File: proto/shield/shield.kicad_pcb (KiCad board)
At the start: 2 copper layers, 68.6 x 124.5 mm, 104 parts, among them J1 ESC_XY, J10 gpio_d, J11 gpio_d, J12 gpio_d, J13 gpio_d, J14 gpio_a, J15 gpio_a, J16 gpio_a, J17 gpio_a, J18 gpio_a, J19 gpio_a, J2 ESC_4Z, J20 gpio_a, J21 gpio_a, J22 5V_IN_A, J23 5V_IN_D, J3 PWM1, J4 PWM2, J5 PWM3, J6 gpio_d, J7 gpio_d, J8 gpio_d, J9 gpio_d, U1 NUCLEO144-F746ZG, U10 LTV-817S, U11 LTV-817S, U12 LTV-817S, U13 LTV-817S, U14 LTV-817S, U15 LTV-817S, U16 LTV-817S, U17 LTV-817S, U2 6N137, U3 6N137, U4 6N137, U5 6N137, U6 6N137, U7 6N137, U8 6N137, U9 6N137

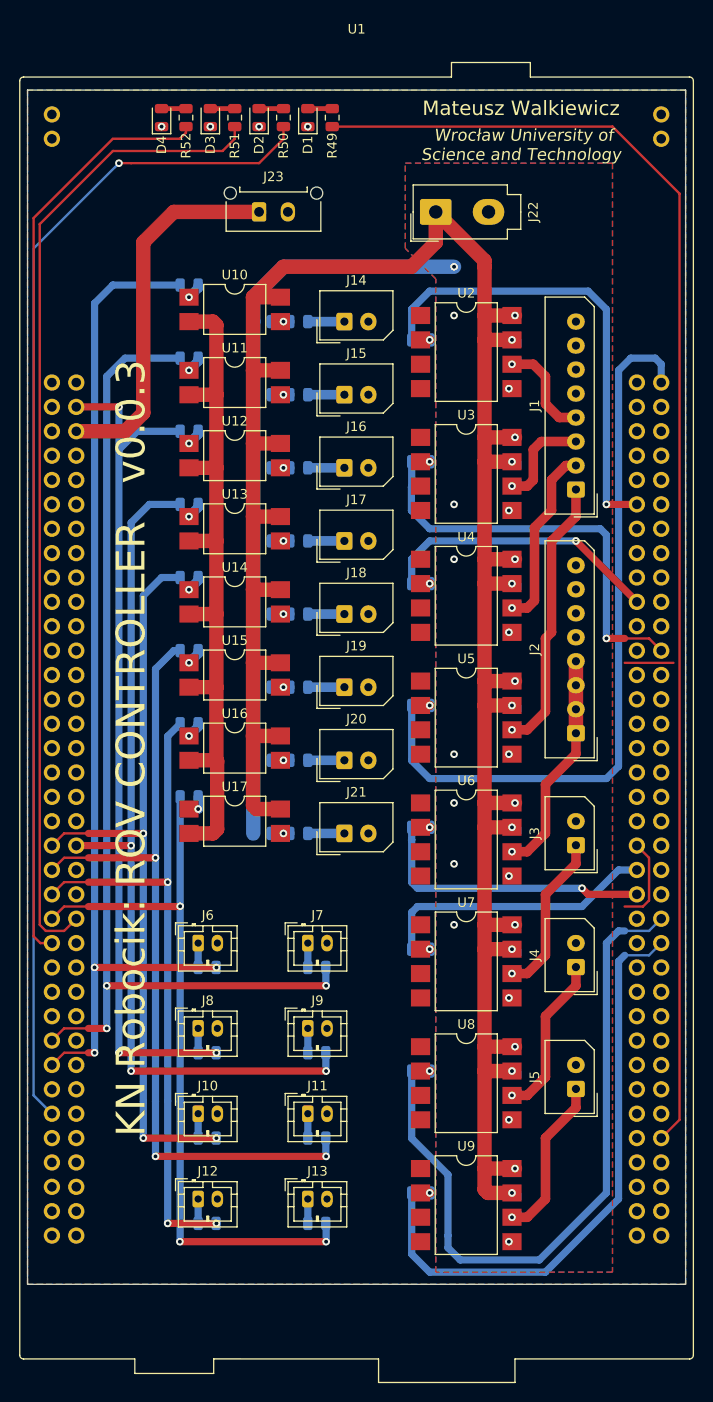
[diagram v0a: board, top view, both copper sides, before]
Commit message: pcb + can + rs232
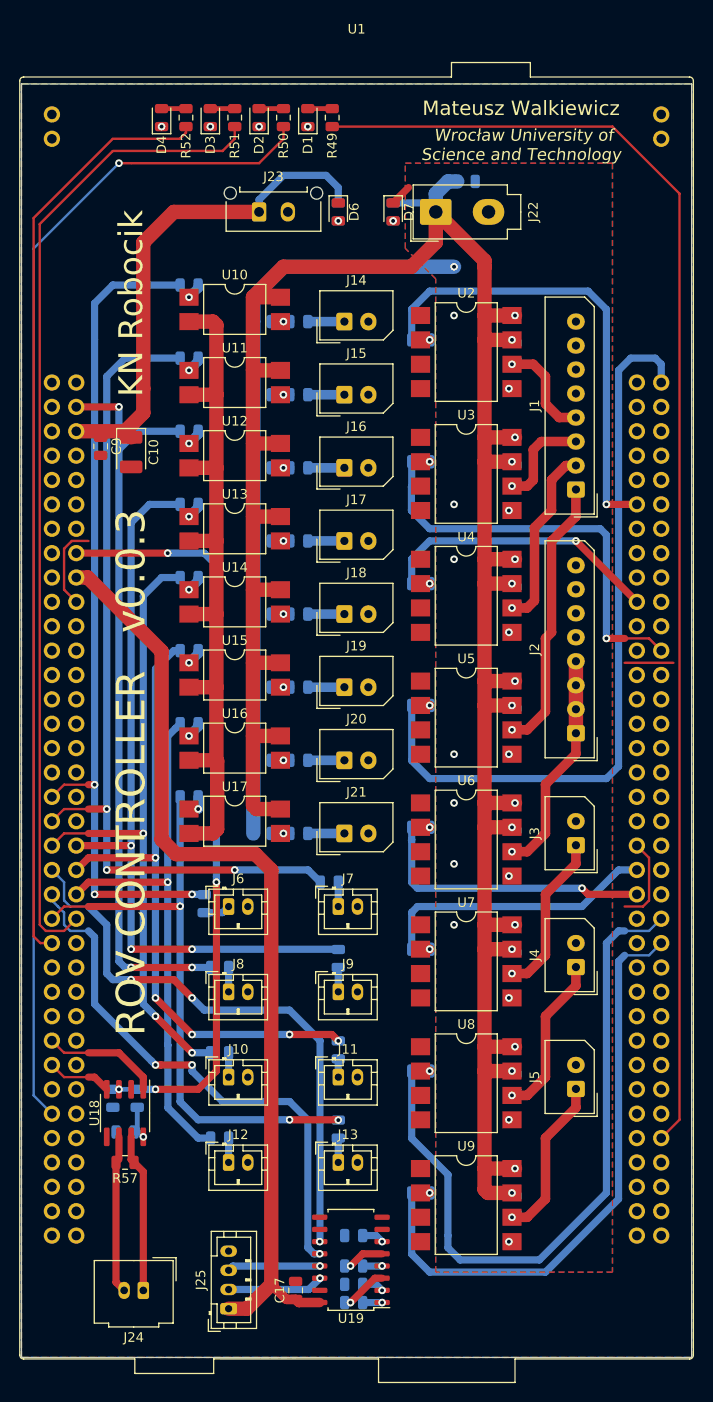
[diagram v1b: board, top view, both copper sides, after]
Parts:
- added C10: 33u, Capacitor_Tantalum_SMD:CP_EIA-3528-21_Kemet-B, F.Cu at (51.4, 78.4)
- added C11: 10u, Capacitor_SMD:C_0805_2012Metric, B.Cu at (86.4, 50.2)
- added C12: 10u, Capacitor_SMD:C_0805_2012Metric, B.Cu at (49.5, 145.7)
- added C13: 47n, Capacitor_SMD:C_0805_2012Metric, B.Cu at (74.6, 167.0)
- added C14: 330n, Capacitor_SMD:C_0805_2012Metric, B.Cu at (74.6, 163.2)
- added C15: 330n, Capacitor_SMD:C_0805_2012Metric, B.Cu at (74.6, 165.1)
- added C16: 330n, Capacitor_SMD:C_0805_2012Metric, B.Cu at (74.6, 160.0)
- added C17: 10u, Capacitor_SMD:C_0805_2012Metric, F.Cu at (68.6, 165.7)
- added C9: 10u, Capacitor_SMD:C_0805_2012Metric, F.Cu at (48.3, 77.8)
- added D6: LED_B, LED_SMD:LED_0805_2012Metric, F.Cu at (73.0, 53.3)
- added D7: LED_B, LED_SMD:LED_0805_2012Metric, F.Cu at (78.7, 53.3)
- added J24: CAN_LINK, Connector_Molex:Molex_MicroClasp_55932-0230_1x02_P2.00mm_Vertical, F.Cu at (52.7, 165.7)
- added J25: Conn_01x04, Connector_JST:JST_PH_B4B-PH-K_1x04_P2.00mm_Vertical, F.Cu at (61.6, 167.6)
- added R53: R, Resistor_SMD:R_0805_2012Metric, B.Cu at (73.0, 53.3)
- added R54: R, Resistor_SMD:R_0805_2012Metric, B.Cu at (78.7, 53.3)
- added R55: 2k2, Resistor_SMD:R_0805_2012Metric, B.Cu at (52.1, 145.7)
- added R56: 10k, Resistor_SMD:R_0805_2012Metric, B.Cu at (50.8, 149.2)
- added R57: 120, Resistor_SMD:R_0805_2012Metric, F.Cu at (50.8, 152.4)
- added U18: SN65HVD230, Package_SO:SOIC-8_3.9x4.9mm_P1.27mm, F.Cu at (50.8, 147.3)
- added U19: MAX3232, Package_SO:SOIC-16_4.55x10.3mm_P1.27mm, F.Cu at (74.3, 162.6)
- U1: value NUCLEO144-F746ZG -> NUCLEO144-F767ZI
- moved R36 10.1 mm to (73.0, 131.1), turned to 90 degrees
- moved R40 10.1 mm to (73.0, 148.9), turned to 90 degrees
- moved R38 9.46 mm to (73.0, 140.7), turned to 90 degrees
- moved R34 8.98 mm to (72.1, 123.2), turned to 180 degrees
- moved R37 8.98 mm to (60.7, 141.0), turned to 180 degrees
- moved R35 8.98 mm to (60.7, 132.1), turned to 180 degrees
- moved R39 8.98 mm to (60.7, 149.9), turned to 180 degrees
- moved R33 6.66 mm to (59.1, 125.4), turned to 90 degrees
- moved J11 4.96 mm to (73.0, 143.5)
- moved J13 4.96 mm to (73.0, 152.4)
- moved J9 4.96 mm to (73.0, 134.6)
- moved J10 4.96 mm to (61.6, 143.5)
- moved J12 4.96 mm to (61.6, 152.4)
- moved J8 4.96 mm to (61.6, 134.6)
- moved J7 4.96 mm to (73.0, 125.7)
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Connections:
- U1 pad 16: (no net) -> +3V3
- U1 pad 18: (no net) -> +5VD
- U1 pad 35: (no net) -> /IO1
- U1 pad 37: (no net) -> /IO2
- U1 pad 41: /IO6 -> /UART_RS_TX
- U1 pad 42: (no net) -> /IO6
- U1 pad 43: /IO7 -> /UART_RS_RX
- U1 pad 44: (no net) -> /IO7
- U1 pad 55: /IO2 -> /CAN1_TX
- U1 pad 57: /IO1 -> /CAN1_RX
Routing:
- net +5VD: track 0.00 -> 99.0 mm
- net +3V3: track 0.00 -> 79.4 mm, vias 0 -> 4
- net /UART_RS_TX: track 0.00 -> 60.4 mm, vias 0 -> 3
- net /UART_RS_RX: track 0.00 -> 56.8 mm, vias 0 -> 3
- net /IO2: track 107.4 -> 88.9 mm
- net /IO6: track 85.2 -> 67.4 mm, vias 3 -> 5
- net /IO1: track 105.5 -> 87.7 mm
- net /CAN_H: track 0.00 -> 16.5 mm
- net /CAN_L: track 0.00 -> 16.1 mm
- net /IO8: track 77.4 -> 63.0 mm
- net /IO7: track 70.3 -> 56.4 mm, vias 3 -> 1
- net +5V: track 38.9 -> 52.5 mm
- net /IO4: track 91.0 -> 77.7 mm
- net /IO5: track 78.8 -> 66.4 mm
- net /CAN1_TX: track 0.00 -> 12.4 mm
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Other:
- board size 68.6 x 124.5 mm -> 69.8 x 132.7 mm
- board text added: "KN Robocik"
- board text added: "ROV CONTROLLER v0.0.3"
- board text removed: "KN Robocik: ROV CONTROLLER v0.0.3"

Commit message: connectors relocation
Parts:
- moved C17 4.73 mm to (72.1, 168.9), turned to 0 degrees
- moved J25 4.62 mm to (66.0, 166.4), turned to 180 degrees
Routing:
- net +5VD: track 99.0 -> 96.1 mm
- net /RS232_RX: track 9.74 -> 11.4 mm
- net /RS232_TX: track 10.0 -> 8.48 mm
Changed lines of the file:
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@@
     (thickness 1.6)
     (drawings 8)
-    (tracks 685)
+    (tracks 688)
     (zones 0)
     (modules 124)
@@
   )
   (setup
-    (last_trace_width 0.25)
+    (last_trace_width 0.75)
     (user_trace_width 0.5)
     (user_trace_width 0.75)
@@
   )
   (module Connector_JST:JST_PH_B4B-PH-K_1x04_P2.00mm_Vertical (layer F.Cu)
-    (at 61.595 167.64 90)
+    (at 66.04 166.37 180)
     (descr "JST PH series connector, B4B-PH-K (http://www.jst-mfg.com/product/pdf/eng/ePH.pdf), generated with kicad-footprint-generator")
     (tags "connector JST PH side entry")
-    (fp_text reference J25 (at 3 -2.9 90) (layer F.SilkS)
+    (fp_text reference J25 (at 3 -2.9) (layer F.SilkS)
       (effects (font (size 1 1) (thickness 0.15)))
     )
-    (fp_text value Conn_01x04 (at 3 4 90) (layer F.Fab)
+    (fp_text value Conn_01x04 (at 3 4) (layer F.Fab)
       (effects (font (size 1 1) (thickness 0.15)))
     )
-    (fp_text user %R (at 3 1.5 90) (layer F.Fab)
+    (fp_text user %R (at 3 1.5) (layer F.Fab)
       (effects (font (size 1 1) (thickness 0.15)))
     )
@@
     (fp_line (start -2.06 2.91) (end 8.06 2.91) (layer F.SilkS) (width 0.12))
     (fp_line (start -2.06 -1.81) (end -2.06 2.91) (layer F.SilkS) (width 0.12))
-    (pad 4 thru_hole oval (at 6 0 90) (size 1.2 1.75) (drill 0.75) (layers *.Cu *.Mask)
+    (pad 4 thru_hole oval (at 6 0 180) (size 1.2 1.75) (drill 0.75) (layers *.Cu *.Mask)
       (net 1 GNDD))
-    (pad 3 thru_hole oval (at 4 0 90) (size 1.2 1.75) (drill 0.75) (layers *.Cu *.Mask)
+    (pad 3 thru_hole oval (at 4 0 180) (size 1.2 1.75) (drill 0.75) (layers *.Cu *.Mask)
       (net 95 /RS232_RX))
-    (pad 2 thru_hole oval (at 2 0 90) (size 1.2 1.75) (drill 0.75) (layers *.Cu *.Mask)
+    (pad 2 thru_hole oval (at 2 0 180) (size 1.2 1.75) (drill 0.75) (layers *.Cu *.Mask)
       (net 94 /RS232_TX))
-    (pad 1 thru_hole roundrect (at 0 0 90) (size 1.2 1.75) (drill 0.75) (layers *.Cu *.Mask) (roundrect_rratio 0.208333)
+    (pad 1 thru_hole roundrect (at 0 0 180) (size 1.2 1.75) (drill 0.75) (layers *.Cu *.Mask) (roundrect_rratio 0.208333)
       (net 83 +5VD))
     (model ${KISYS3DMOD}/Connector_JST.3dshapes/JST_PH_B4B-PH-K_1x04_P2.00mm_Vertical.wrl
@@
   )
   (module Capacitor_SMD:C_0805_2012Metric (layer F.Cu)
-    (at 68.58 165.735 90)
+    (at 72.0875 168.91)
     (descr "Capacitor SMD 0805 (2012 Metric), square (rectangular) end terminal, IPC_7351 nominal, (Body size source: https://docs.google.com/spreadsheets/d/1BsfQQcO9C6DZCsRaXUlFlo91Tg2WpOkGARC1WS5S8t0/edit?usp=sharing), generated with kicad-footprint-generator")
     (tags capacitor)
     (attr smd)
-    (fp_text reference C17 (at 0 -1.65 90) (layer F.SilkS)
+    (fp_text reference C17 (at 0 -1.65) (layer F.SilkS)
       (effects (font (size 1 1) (thickness 0.15)))
     )
-    (fp_text value 10u (at 0 1.65 90) (layer F.Fab)
+    (fp_text value 10u (at 0 1.65) (layer F.Fab)
       (effects (font (size 1 1) (thickness 0.15)))
     )
-    (fp_text user %R (at 0 0 90) (layer F.Fab)
+    (fp_text user %R (at 0 0) (layer F.Fab)
       (effects (font (size 0.5 0.5) (thickness 0.08)))
     )
@@
     (fp_line (start -1 -0.6) (end 1 -0.6) (layer F.Fab) (width 0.1))
     (fp_line (start -1 0.6) (end -1 -0.6) (layer F.Fab) (width 0.1))
-    (pad 2 smd roundrect (at 0.9375 0 90) (size 0.975 1.4) (layers F.Cu F.Paste F.Mask) (roundrect_rratio 0.25)
+    (pad 2 smd roundrect (at 0.9375 0) (size 0.975 1.4) (layers F.Cu F.Paste F.Mask) (roundrect_rratio 0.25)
       (net 1 GNDD))
-    (pad 1 smd roundrect (at -0.9375 0 90) (size 0.975 1.4) (layers F.Cu F.Paste F.Mask) (roundrect_rratio 0.25)
+    (pad 1 smd roundrect (at -0.9375 0) (size 0.975 1.4) (layers F.Cu F.Paste F.Mask) (roundrect_rratio 0.25)
       (net 83 +5VD))
     (model ${KISYS3DMOD}/Capacitor_SMD.3dshapes/C_0805_2012Metric.wrl
@@
   (segment (start 54.61 118.745) (end 54.61 99.127919) (width 1.5) (layer F.Cu) (net 83))
   (segment (start 56.134 120.269) (end 54.61 118.745) (width 1.5) (layer F.Cu) (net 83))
-  (segment (start 63.5 167.64) (end 66.04 165.1) (width 1.5) (layer F.Cu) (net 83))
   (segment (start 66.04 121.92) (end 64.389 120.269) (width 1.5) (layer F.Cu) (net 83))
   (segment (start 64.389 120.269) (end 56.134 120.269) (width 1.5) (layer F.Cu) (net 83))
-  (segment (start 61.595 167.64) (end 63.5 167.64) (width 1.5) (layer F.Cu) (net 83))
   (segment (start 66.04 165.1) (end 66.04 121.92) (width 1.5) (layer F.Cu) (net 83))
-  (segment (start 67.6125 166.6725) (end 66.04 165.1) (width 1) (layer F.Cu) (net 83))
-  (segment (start 68.58 166.6725) (end 67.6125 166.6725) (width 1) (layer F.Cu) (net 83))
-  (segment (start 68.9075 167) (end 68.58 166.6725) (width 1) (layer F.Cu) (net 83))
-  (segment (start 71.09 167) (end 68.9075 167) (width 1) (layer F.Cu) (net 83))
+  (segment (start 66.04 165.1) (end 66.04 166.37) (width 1.5) (layer F.Cu) (net 83))
+  (segment (start 66.04 166.37) (end 66.675 167.005) (width 1.5) (layer F.Cu) (net 83))
+  (segment (start 66.68 167) (end 69.21 167) (width 1.5) (layer F.Cu) (net 83))
+  (segment (start 66.675 167.005) (end 66.68 167) (width 1.5) (layer F.Cu) (net 83))
+  (segment (start 71.09 167) (end 69.21 167) (width 0.75) (layer F.Cu) (net 83))
+  (segment (start 71.15 167.06) (end 71.09 167) (width 0.75) (layer F.Cu) (net 83))
+  (segment (start 71.15 168.91) (end 71.15 167.06) (width 0.75) (layer F.Cu) (net 83))
   (segment (start 43.18 142.24) (end 44.45 143.51) (width 0.25) (layer F.Cu) (net 84))
   (segment (start 44.45 143.51) (end 46.99 143.51) (width 0.25) (layer F.Cu) (net 84))
@@
   (segment (start 67.945 136.525) (end 71.12 139.7) (width 0.75) (layer B.Cu) (net 93))
   (segment (start 71.12 139.7) (end 71.12 160.585) (width 0.75) (layer B.Cu) (net 93))
-  (segment (start 71.09 164.46) (end 71.115 164.46) (width 0.75) (layer F.Cu) (net 94))
   (via (at 71.12 164.465) (size 0.8) (drill 0.4) (layers F.Cu B.Cu) (net 94))
+  (segment (start 71.09 164.46) (end 71.115 164.46) (width 0.75) (layer F.Cu) (net 94))
   (segment (start 71.115 164.46) (end 71.12 164.465) (width 0.75) (layer F.Cu) (net 94))
-  (segment (start 69.945 165.64) (end 61.595 165.64) (width 0.75) (layer B.Cu) (net 94))
-  (segment (start 71.12 164.465) (end 69.945 165.64) (width 0.75) (layer B.Cu) (net 94))
+  (segment (start 71.12 164.465) (end 64.955 164.465) (width 0.75) (layer B.Cu) (net 94))
+  (segment (start 64.04 165.38) (end 64.04 166.37) (width 0.75) (layer B.Cu) (net 94))
+  (segment (start 64.955 164.465) (end 64.04 165.38) (width 0.75) (layer B.Cu) (net 94))
   (via (at 71.12 163.195) (size 0.8) (drill 0.4) (layers F.Cu B.Cu) (net 95))
   (segment (start 71.09 163.19) (end 71.115 163.19) (width 0.75) (layer F.Cu) (net 95))
   (segment (start 71.115 163.19) (end 71.12 163.195) (width 0.75) (layer F.Cu) (net 95))
-  (segment (start 62.04 163.195) (end 61.595 163.64) (width 0.75) (layer B.Cu) (net 95))
-  (segment (start 71.12 163.195) (end 62.04 163.195) (width 0.75) (layer B.Cu) (net 95))
+  (segment (start 71.12 163.195) (end 63.5 163.195) (width 0.75) (layer B.Cu) (net 95))
+  (segment (start 62.04 164.655) (end 62.04 166.37) (width 0.75) (layer B.Cu) (net 95))
+  (segment (start 63.5 163.195) (end 62.04 164.655) (width 0.75) (layer B.Cu) (net 95))
   (zone (net 2) (net_name GNDA) (layer B.Cu) (hatch edge 0.508)
     (priority 1)

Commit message: new layout
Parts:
- moved R1 17.8 mm to (99.4, 65.4), turned to 0 degrees
- moved R11 17.8 mm to (99.4, 128.9), turned to 0 degrees
- moved R12 17.8 mm to (99.4, 141.6), turned to 0 degrees
- moved R13 17.8 mm to (99.4, 154.3), turned to 0 degrees
- moved R2 17.8 mm to (99.4, 78.1), turned to 0 degrees
- moved R3 17.8 mm to (99.4, 90.8), turned to 0 degrees
- moved R4 17.8 mm to (99.4, 103.5), turned to 0 degrees
- moved R5 17.8 mm to (99.4, 116.2), turned to 0 degrees
- moved J5 14.5 mm to (85.1, 137.8)
- moved J4 13.5 mm to (85.1, 127.6)
- moved J3 12.8 mm to (85.1, 117.4)
- moved J1 12.7 mm to (85.1, 81.6)
- moved J2 12.7 mm to (85.1, 107.0)
- moved U3 9.09 mm to (94.6, 76.8), turned to 180 degrees
- moved U4 9.09 mm to (94.6, 89.5), turned to 180 degrees
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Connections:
- U1 pad 113: /TIM4_CH2 -> /TIM4_CH1
- U1 pad 115: /TIM4_CH1 -> /TIM4_CH2
- U1 pad 35: /IO1 -> /IO2
- U1 pad 37: /IO2 -> /IO3
- U1 pad 39: /IO5 -> /IO4
- U1 pad 4: /IO3 -> /IO1
- U1 pad 40: /IO4 -> /IO5
- U1 pad 74: /TIM3_CH4 -> /TIM3_CH1
- U1 pad 83: /TIM3_CH1 -> /TIM3_CH2
- U1 pad 96: /TIM3_CH2 -> /TIM3_CH4
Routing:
- net /TIM3_CH4: track 77.0 -> 8.89 mm
- net /TIM4_CH3: track 72.7 -> 18.7 mm
- net /TIM3_CH1: track 48.6 -> 11.0 mm, vias 1 -> 0
- net /TIM3_CH2: track 43.5 -> 8.81 mm, vias 1 -> 0
- net /TIM4_CH4: track 61.9 -> 29.3 mm
- net /TIM3_CH3: track 29.4 -> 6.27 mm, vias 1 -> 0
- net GNDD: track 98.9 -> 75.9 mm
- net /TIM4_CH2: track 29.1 -> 6.80 mm
- net /TIM4_CH1: track 29.8 -> 8.05 mm, vias 1 -> 0
- net +5VA: track 267.7 -> 285.5 mm, vias 16 -> 8
- net +3V3: track 79.4 -> 91.3 mm
- net /TIM3_CH4_A: track 29.2 -> 22.5 mm
- net /TIM4_CH1_A: track 24.0 -> 17.3 mm
- net /TIM3_CH3_A: track 19.6 -> 13.3 mm
- net /TIM3_CH2_A: track 10.9 -> 5.21 mm
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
